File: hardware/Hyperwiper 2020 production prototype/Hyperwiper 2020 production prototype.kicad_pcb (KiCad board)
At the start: 2 copper layers, 123.8 x 65.8 mm, 26 parts, among them J1 Conn_01x05, Q2 2N3904, Q3 IRF4905, SW1 SW_DPDT_x2, SW2 SW_Reed, U1 Teensy4.0, U3 Voltage regulator

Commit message: Changed for  V2.3.0
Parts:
- C2, C3: footprint Capacitor_THT:CP_Radial_D10.0mm_P5.00mm -> Capacitor_THT:CP_Radial_D5.0mm_P2.50mm
- D1, D2: footprint LED_THT:LED_D5.0mm-4_RGB -> LED_THT:LED_D5.0mm-4_RGB_Wide_Pins
- D4: footprint Diode_THT:D_DO-15_P15.24mm_Horizontal -> Diode_THT:D_DO-35_SOD27_P10.16mm_Horizontal
- RV1: moved to F.Cu
- SW1: footprint Button_Switch_THT:SW_NKK_GW12LJP -> Button_Switch_THT:SW_NKK_G1xJP
- moved RV1 5.07 mm to (154.4, 89.5)
- moved SW1 4.11 mm to (192.0, 106.0), turned to 90 degrees
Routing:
- net /reed: track 143.9 -> 0.00 mm
- net /5V: track 106.3 -> 0.00 mm
- net /motor_PWM: track 92.5 -> 0.00 mm
- net +3V3: track 84.8 -> 0.00 mm
- net /Pot: track 72.1 -> 0.00 mm
- net TX-1: track 70.0 -> 0.00 mm
- net Net-(D2-Pad1): track 65.7 -> 0.00 mm
- net Net-(D1-Pad4): track 64.0 -> 0.00 mm
- net RX-1: track 63.4 -> 0.00 mm
- net Net-(D1-Pad3): track 57.9 -> 0.00 mm
- net Net-(D1-Pad1): track 56.3 -> 0.00 mm
- net /M_LED_b: track 56.3 -> 0.00 mm
- net Net-(D4-Pad1): track 56.1 -> 0.00 mm
- net TX-2: track 55.5 -> 0.00 mm
- net Net-(D2-Pad3): track 53.2 -> 0.00 mm
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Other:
- board text added: "2021-03-25 for V2.3.0 - changed footprint diode - chnage foot print for LEDS - changed footprint switch (still need better check) 2021-03-07 for V2.2.7 Note for next version: - reverce the pin for connector - switch footprint fix - 90 degree swith better - bigger hole for switch - resitor pack?"
- board text added: "HyperWiperPrototype V2.3.0"
- board text removed: "2020-03-07 for V2.2.7 Note for next version: - reverce the pin for connector - switch footprint fix - 90 degree swith better - bigger hole for switch - resitor pack?"
- board text removed: "HyperWiperPrototype V2.2.7"

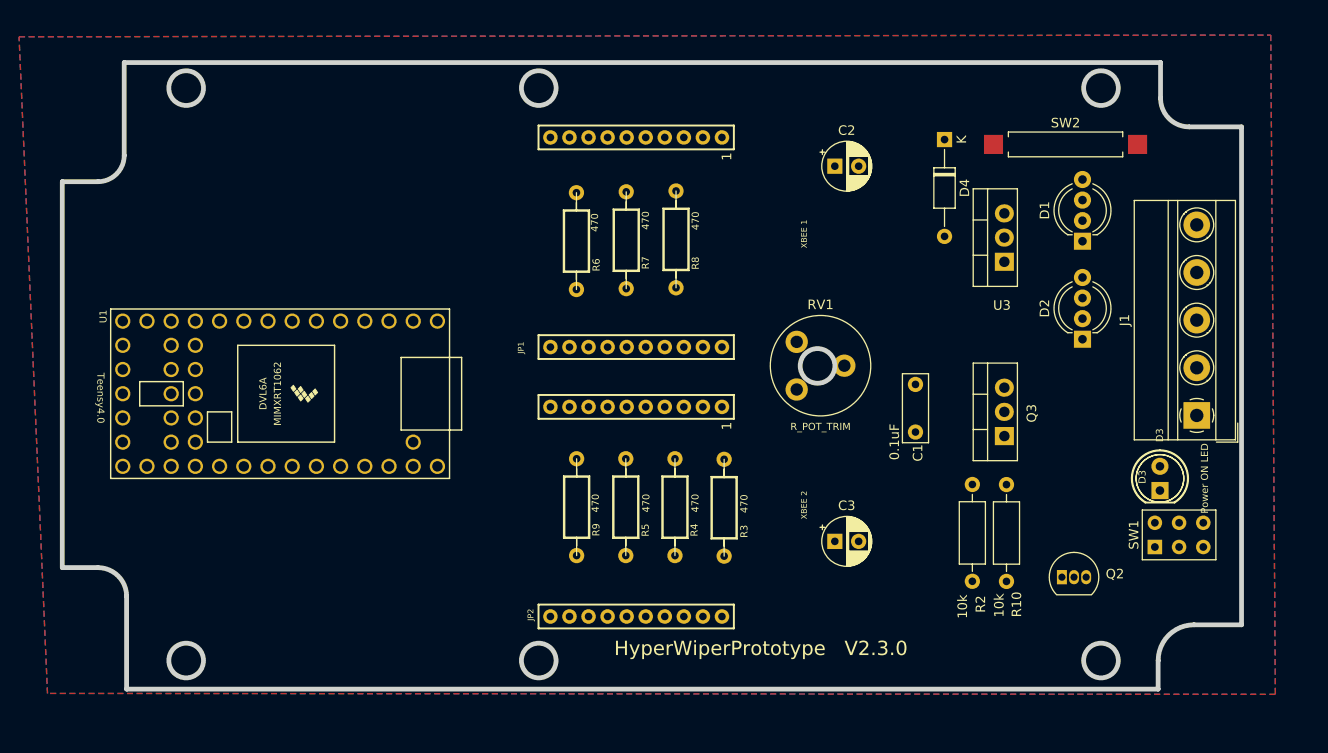
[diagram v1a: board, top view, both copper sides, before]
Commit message: Updated for MOSFET hookup mistake
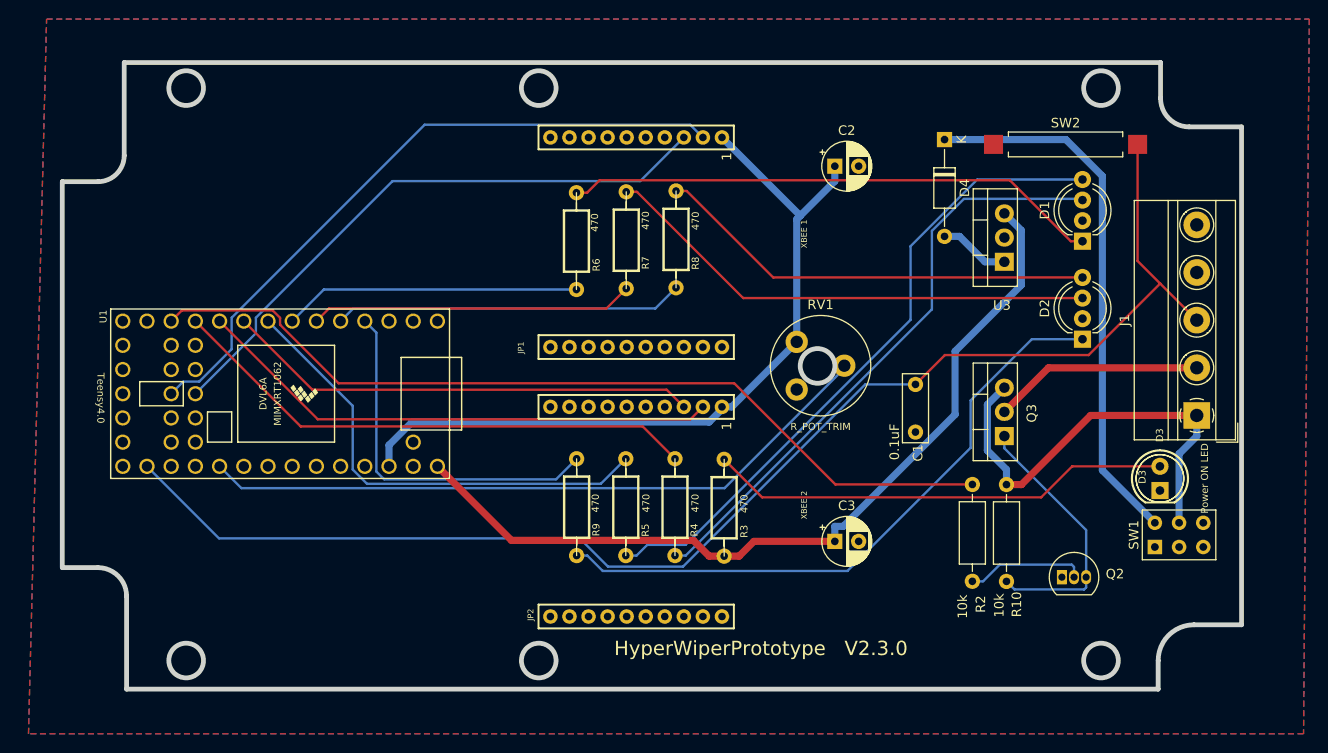
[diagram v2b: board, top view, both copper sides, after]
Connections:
- J1 pad 1: Net-(D5-Pad1) -> Net-(J1-Pad1)
- J1 pad 2: Net-(D5-Pad2) -> Net-(J1-Pad2)
- Q3 pad 2: Net-(D5-Pad1) -> Net-(J1-Pad2)
- Q3 pad 3: Net-(D5-Pad2) -> Net-(J1-Pad1)
- R10 pad 2: Net-(D5-Pad1) -> Net-(J1-Pad1)
- SW1 pad 1: Net-(Q2-Pad3) -> (no net)
- SW1 pad 2: GND -> (no net)
- SW1 pad 3: unconnected-(SW1-Pad3) -> (no net)
- SW1 pad 5: Net-(D5-Pad1) -> Net-(J1-Pad1)
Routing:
- net /reed: track 0.00 -> 144.0 mm
- net /motor_PWM: track 0.00 -> 92.5 mm
- net /5V: track 0.00 -> 90.0 mm
- net +3V3: track 0.00 -> 81.4 mm
- net /Pot: track 0.00 -> 72.0 mm
- net TX-1: track 0.00 -> 70.0 mm
- net Net-(D1-Pad4): track 0.00 -> 68.8 mm
- net Net-(D2-Pad1): track 0.00 -> 66.7 mm
- net RX-1: track 0.00 -> 63.3 mm
- net Net-(D1-Pad3): track 0.00 -> 63.1 mm
- net Net-(D4-Pad1): track 0.00 -> 56.8 mm
- net /M_LED_b: track 0.00 -> 56.3 mm
- net Net-(D1-Pad1): track 0.00 -> 56.3 mm
- net TX-2: track 0.00 -> 55.5 mm
- net Net-(D2-Pad3): track 0.00 -> 52.5 mm
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
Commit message: Updated boards with resistor block and moved parts
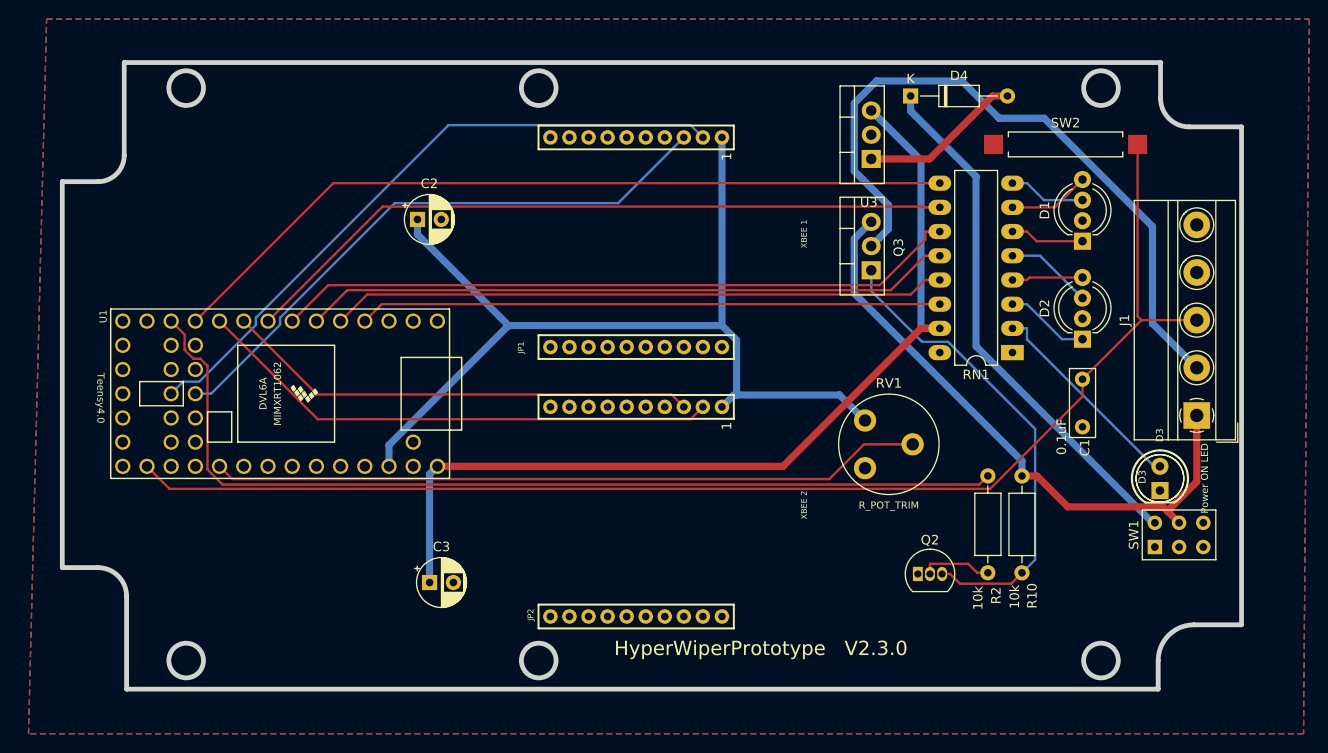
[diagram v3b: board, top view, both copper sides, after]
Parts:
- removed R3, R4, R5, R6, R7, R8, R9: 470, Resistor_THT:R_Axial_DIN0207_L6.3mm_D2.5mm_P10.16mm_Horizontal
- added RN1: R_Pack08, Package_DIP:DIP-16_W7.62mm_LongPads, F.Cu at (177.1, 85.6)
- moved C2 44.2 mm to (114.6, 71.6)
- moved C3 42.7 mm to (115.9, 109.7)
- moved Q3 22.3 mm to (162.2, 77.0)
- moved U3 17.7 mm to (162.2, 65.3)
- moved C1 17.5 mm to (184.4, 88.4)
- moved Q2 15.1 mm to (167.1, 108.8)
- moved RV1 10.9 mm to (161.6, 97.7)
- moved D4 5.79 mm to (166.4, 58.7), turned to 0 degrees
- moved R10 1.86 mm to (178.1, 108.7)
- moved R2 1.86 mm to (174.5, 98.5)
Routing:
- net Net-(D1-Pad4): track 68.8 -> 8.56 mm
- net Net-(D2-Pad1): track 66.7 -> 8.87 mm
- net Net-(D1-Pad3): track 63.1 -> 8.09 mm
- net Net-(J1-Pad2): track 22.1 -> 72.6 mm
- net Net-(D1-Pad1): track 56.3 -> 7.77 mm
- net Net-(D2-Pad3): track 52.5 -> 9.19 mm
- net /M_LED_r: track 31.2 -> 72.4 mm
- net Net-(D2-Pad4): track 46.4 -> 7.46 mm
- net /B_LED_b: track 33.9 -> 68.3 mm
- net /B_LED_g: track 36.6 -> 64.7 mm
- net /M_LED_b: track 56.3 -> 84.1 mm
- net Net-(D3-Pad2): track 48.7 -> 22.1 mm
- net /M_LED_g: track 49.6 -> 75.5 mm
- net /B_LED_r: track 38.5 -> 61.1 mm
- net Net-(Q2-Pad3): track 28.2 -> 50.3 mm
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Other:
- outline, holes or cut-outs redrawn

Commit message: Updated board to V2.4.0 with relay and usb out
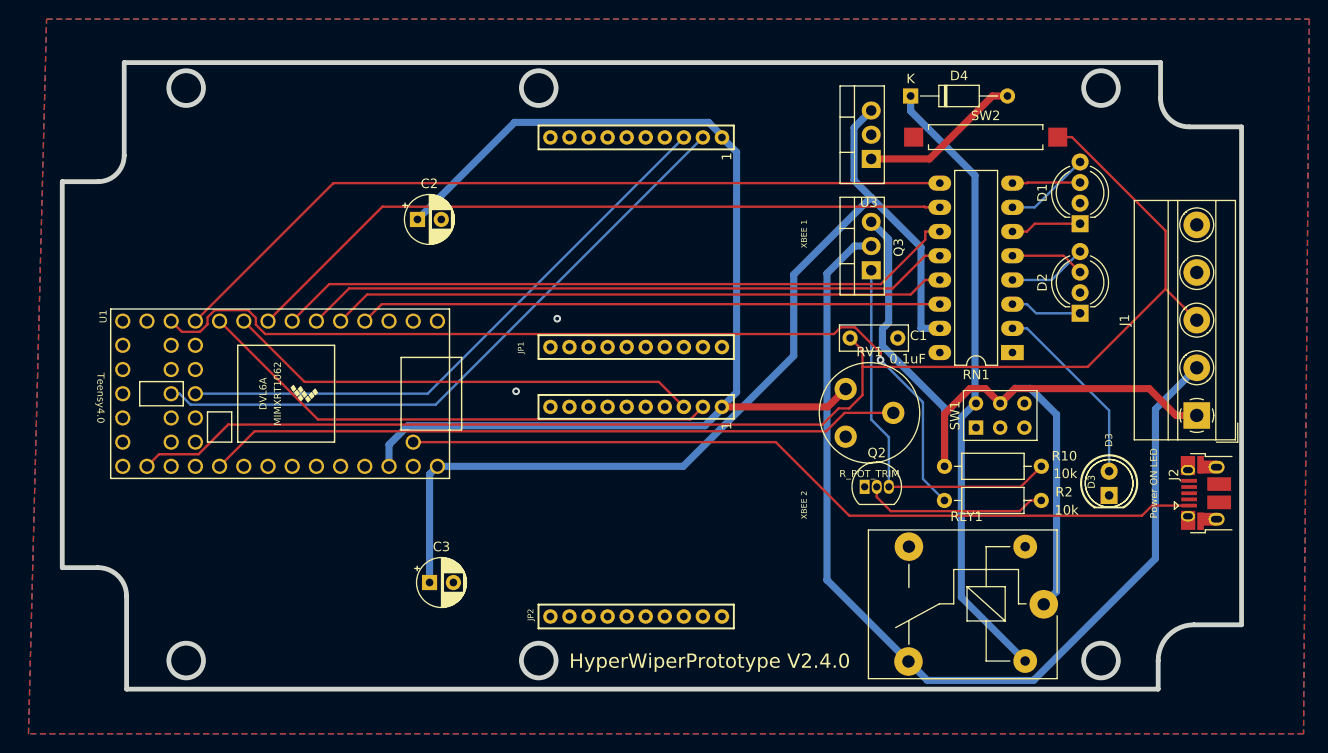
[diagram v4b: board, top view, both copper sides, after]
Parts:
- added J2: USB_B, Connector_USB:USB_Micro-B_Amphenol_10103594-0001LF_Horizontal, F.Cu at (197.4, 100.3)
- added RLY1: JSM1-12V-5, Relay_THT:Relay_SPDT_SANYOU_SRD_Series_Form_C, F.Cu at (180.3, 112.0)
- moved C1 24.8 mm to (160.0, 84.1), turned to 0 degrees
- moved SW1 22.6 mm to (173.2, 93.5)
- moved R10 11.4 mm to (180.1, 97.5), turned to 180 degrees
- moved Q2 10.7 mm to (161.5, 99.7)
- moved SW2 8.42 mm to (174.2, 63.0)
- moved D3 5.36 mm to (187.2, 100.6)
- moved R2 5.23 mm to (169.9, 101.1), turned to 0 degrees
- moved RV1 3.88 mm to (159.6, 94.4)
- moved D2 2.74 mm to (184.2, 81.5)
- moved D1 1.86 mm to (184.2, 72.1)
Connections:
- U1 pad 34: unconnected-(U1-Pad34) -> Net-(U1-Pad34)
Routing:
- net Net-(U1-Pad34): track 0.00 -> 85.1 mm
- net Net-(RLY1-Pad4): track 72.6 -> 103.9 mm
- net Net-(J1-Pad1): track 64.5 -> 93.1 mm
- net +3V3: track 101.8 -> 119.2 mm
- net Net-(Q2-Pad2): track 7.54 -> 19.4 mm
- net Net-(D4-Pad1): track 55.5 -> 65.6 mm
- net Net-(Q2-Pad3): track 50.3 -> 40.4 mm
- net /reed: track 138.2 -> 146.0 mm
- net /5V: track 98.2 -> 103.2 mm
- net /motor_PWM: track 100.5 -> 97.4 mm, vias 0 -> 1
- net Net-(D3-Pad2): track 22.1 -> 20.1 mm
- net /Pot: track 74.8 -> 73.0 mm
- net Net-(D2-Pad3): track 9.19 -> 7.81 mm
- net Net-(D2-Pad1): track 8.87 -> 7.49 mm
- net Net-(D1-Pad3): track 8.09 -> 7.12 mm
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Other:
- board text added: "2021-04-15 vV.4.0 (final) - for next version usb to outside for easier programming and USB power disconnected external - check footprint and pads numbering USB 2021-03-25 for V2.3.0 - changed footprint diode - chnage foot print for LEDS - changed footprint switch (still need better check) 2021-03-07 for V2.2.7 Note for next version: - reverce the pin for connector - switch footprint fix - 90 degr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"
- board text added: "HyperWiperPrototype V2.4.0"
- board text removed: "2021-03-25 for V2.3.0 - changed footprint diode - chnage foot print for LEDS - changed footprint switch (still need better check) 2021-03-07 for V2.2.7 Note for next version: - reverce the pin for connector - switch footprint fix - 90 degree swith better - bigger hole for switch - resitor pack?"
- board text removed: "HyperWiperPrototype V2.3.0"

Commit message: Updated board
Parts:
- J2: footprint Connector_USB:USB_Micro-B_Amphenol_10103594-0001LF_Horizontal -> digikey-footprints:USB_Micro_B_Male_UJ2-MIBH-4-SMT-TR
- moved J2 3.02 mm to (200.4, 100.3), turned to 180 degrees
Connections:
- J1 pad 2: Net-(RLY1-Pad4) -> (no net)
- J2 pad 2: Net-(U1-Pad53) -> unconnected-(J2-Pad2)
- J2 pad 4: GND -> Net-(J2-Pad4)
- J2 pad 5: unconnected-(J2-Pad5) -> GND
- Q3 pad 2: Net-(RLY1-Pad4) -> (no net)
- RLY1 pad 4: Net-(RLY1-Pad4) -> (no net)
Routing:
- net /reed: track 146.0 -> 0.00 mm
- net +3V3: track 119.2 -> 0.00 mm
- net Net-(RLY1-Pad4): track 103.9 -> 0.00 mm
- net /5V: track 103.2 -> 0.00 mm
- net /motor_PWM: track 97.4 -> 0.00 mm, vias 1 -> 0
- net Net-(J1-Pad1): track 93.1 -> 0.00 mm
- net Net-(J2-Pad1): track 85.1 -> 0.00 mm
- net /M_LED_b: track 84.1 -> 0.00 mm
- net /M_LED_g: track 75.5 -> 0.00 mm
- net /Pot: track 73.0 -> 0.00 mm
- net /M_LED_r: track 72.4 -> 0.00 mm
- net /B_LED_b: track 68.3 -> 0.00 mm
- net TX-1: track 67.9 -> 0.00 mm
- net Net-(D4-Pad1): track 65.6 -> 0.00 mm
- net /B_LED_g: track 64.7 -> 0.00 mm
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
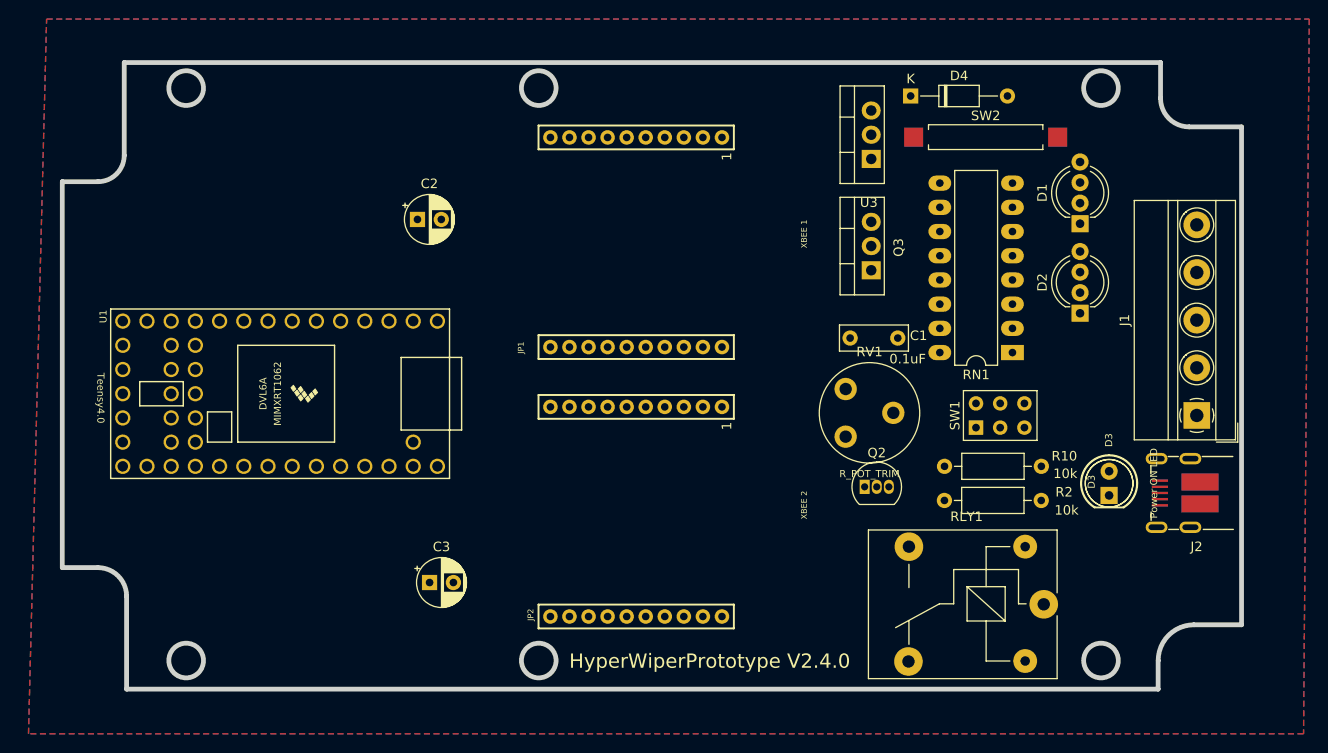
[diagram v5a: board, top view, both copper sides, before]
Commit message: updated code for mosfet
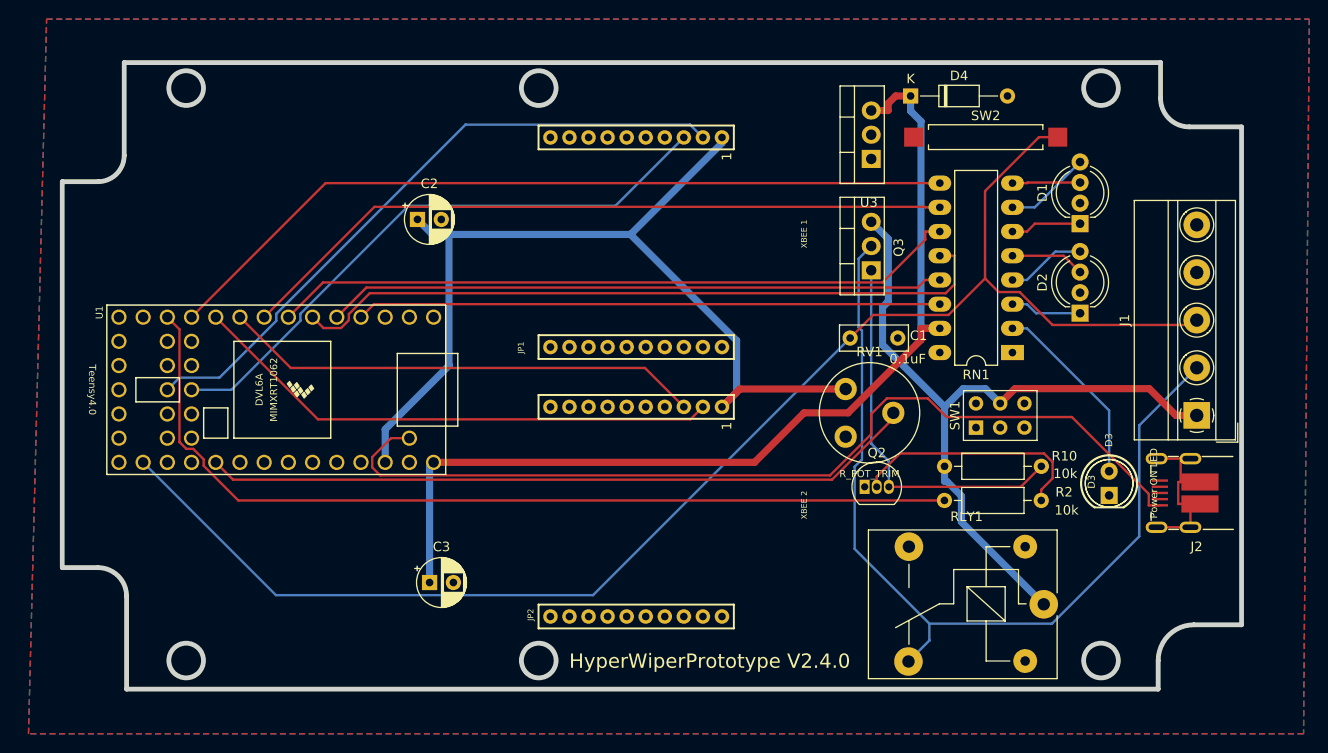
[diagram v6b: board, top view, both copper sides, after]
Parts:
- U1: footprint Teensy:Teensy40 -> Hyperwiper 2020 production prototype all:Teensy40
- moved U1 0.58 mm to (99.8, 89.5)
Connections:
- D4 pad 1: Net-(D4-Pad1) -> /5V
- D4 pad 2: Net-(D4-Pad2) -> (no net)
- J1 pad 2: (no net) -> Net-(J1-Pad2)
- Q3 pad 2: (no net) -> Net-(J1-Pad2)
- RLY1 pad 4: (no net) -> Net-(J1-Pad2)
- RLY1 pad 5: Net-(D4-Pad1) -> (no net)
- SW1 pad 6: Net-(D4-Pad1) -> (no net)
- U3 pad 1: Net-(D4-Pad2) -> (no net)
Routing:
- net /reed: track 0.00 -> 151.5 mm
- net /5V: track 0.00 -> 104.5 mm
- net +3V3: track 0.00 -> 101.0 mm
- net Net-(J2-Pad1): track 0.00 -> 98.8 mm
- net /motor_PWM: track 0.00 -> 96.8 mm
- net Net-(J1-Pad2): track 0.00 -> 94.8 mm
- net /M_LED_b: track 0.00 -> 84.3 mm
- net Net-(J1-Pad1): track 0.00 -> 78.0 mm
- net /M_LED_g: track 0.00 -> 75.7 mm
- net /Pot: track 0.00 -> 75.1 mm
- net /B_LED_b: track 0.00 -> 74.6 mm
- net /M_LED_r: track 0.00 -> 72.6 mm
- net TX-1: track 0.00 -> 68.7 mm
- net /B_LED_g: track 0.00 -> 64.9 mm
- net RX-1: track 0.00 -> 63.1 mm
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
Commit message: Updated schematic for N-CH MOSFET  switching
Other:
- board text added: "HyperWiper Prototype V2.4.0"
- board text removed: "HyperWiperPrototype V2.4.0"
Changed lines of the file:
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@@
   (gr_arc (start 81.095 111.165) (end 81.095 108.165) (angle 90) (layer "Edge.Cuts") (width 0.5))
   (gr_line (start 192.345 117.915) (end 192.345 120.915) (layer "Edge.Cuts") (width 0.5))
-  (gr_text "HyperWiperPrototype   V2.4.0\n   \n" (at 173.99 110.236) (layer "B.SilkS")
-    (effects (font (size 1.5 1.5) (thickness 0.3)) (justify mirror))
+  (gr_text "HyperWiper Prototype   V2.4.0\n   \n" (at 173.99 110.236) (layer "B.SilkS")
+    (effects (font (size 1.4 1.4) (thickness 0.3)) (justify mirror))
   )
-  (gr_text "HyperWiperPrototype V2.4.0\n\n\n" (at 145.288 120.396) (layer "F.SilkS")
-    (effects (font (size 1.5 1.5) (thickness 0.3)))
+  (gr_text "HyperWiper Prototype V2.4.0\n\n\n" (at 145.288 120.396) (layer "F.SilkS")
+    (effects (font (size 1.4 1.4) (thickness 0.3)))
   )
   (gr_text "2021-04-15 vV.4.0 (final)\n- for next version usb to outside for easier programming \n   and USB power disconnected external\n- check footprint and pads numbering USB\n\n2021-03-25 for V2.3.0\n\n- changed footprint diode\n- chnage foot print for LEDS\n- changed footprint switch (still need better check)\n\n2021-03-07 for V2.2.7\n\nNote for next version:\n- reverce the pin for connector\n- switch  footprint fix\n- 90 degree swith better\n- bigger hole for switch\n- resitor pack?\n" (at 217.8 105.6) (layer "Eco2.User")
